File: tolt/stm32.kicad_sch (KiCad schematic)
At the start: 16 parts, among them U1 STM32F405RGTx, Y1 8m

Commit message: modified:   tolt/inter.kicad_sch 	modified:   tolt/stm32.kicad_sch
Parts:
- renumbered C12 to C10, C5 to C11, C6 to C12, C7 to C5, C8 to C6, C9 to C7, C10 to C8, C11 to C9
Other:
- moved on the sheet: C1, C10, C2, C3, C4, C5, C6, C7, C8, C9

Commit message: new file:   tolt/powerstage.kicad_sch 	modified:   tolt/stm32.kicad_sch 	modified:   tolt/tolt.kicad_pro 	modified:   tolt/tolt.kicad_sch
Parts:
- added C27, C28, C31, C32, C33, C34, C37, C38, C39: 100n, Capacitor_SMD:C_0402_1005Metric, symbol Device:C
- added C29, C36, C41: 15n, Capacitor_SMD:C_0603_1608Metric, symbol Device:C
- added C30, C35, C40: 1n, Capacitor_SMD:C_0603_1608Metric, symbol Device:C
- added R33, R34, R35: 1k, Resistor_SMD:R_0603_1608Metric, symbol Device:R
- added U10, U6, U8: MC74VHC1GT66, Package_TO_SOT_SMD:SOT-353_SC-70-5, symbol Analog_Switch:TS5A3166DCKR
- added U5, U7, U9: ~, Package_TO_SOT_SMD:SOT-23-8, symbol Amplifier_Current:INA241
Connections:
- net CURRENT_1: now also C30.1, R33.2, U10.1
- net CURRENT_2: now also C35.1, R34.2, U6.1
- net CURRENT_3: now also C40.1, R35.2, U8.1
- net GND: now also C27.1, C28.1, C29.2, C30.2, C31.1, C32.1, C33.1, C34.1, C35.2, C36.2, C37.1, C38.1, C39.1, C40.2, C41.2, U10.3 (GND), U5.2 (GND), U5.3 (REF2), U6.3 (GND), U7.2 (GND), U7.3 (REF2), U8.3 (GND), U9.2 (GND), U9.3 (REF2)
- net VCC: now also C27.2, C28.2, C31.2, C32.2, C33.2, C34.2, C37.2, C38.2, C39.2, U10.5 (V+), U5.6 (Vs), U5.7 (REF1), U6.5 (V+), U7.6 (Vs), U7.7 (REF1), U8.5 (V+), U9.6 (Vs), U9.7 (REF1)
- new net: R33.1, U5.5 (OUT)
- new net: C36.1, U6.2
- new net: R34.1, U7.5 (OUT)
- new net: C29.1, U10.2
- new net: R35.1, U9.5 (OUT)
- new net: C41.1, U8.2
- new net CURR_FILTER: U10.4, U6.4, U8.4
- new net sens_a+: U5.8 (IN+)
- new net sens_a-: U5.1 (IN-)
- new net sens_b+: U7.8 (IN+)
- new net sens_b-: U7.1 (IN-)
- new net sens_c+: U9.8 (IN+)
- new net sens_c-: U9.1 (IN-)
- no-connect marks 4 -> 7
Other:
- moved on the sheet: C1, C10, C11, C12, C13, C14, C2, C3, C4, C5, C6, C7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

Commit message: i hate RC Filters
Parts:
- added J14: BOOT0, x`, symbol Connector_Generic:Conn_01x02
- added J15: NRST, Jumper:SolderJumper-2_P1.3mm_Open_RoundedPad1.0x1.5mm, symbol Connector_Generic:Conn_01x02
- added R38, R39: 10k, Resistor_SMD:R_0603_1608Metric, symbol Device:R_Small
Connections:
- net GND: now also J15.1 (Pin_1), R38.2
- net at U1.60 (BOOT0): now also J14.2 (Pin_2), R38.1
- net at U1.7 (NRST): now also J15.2 (Pin_2), R39.2
- net sens_a+ renamed SENS_A+
- net sens_a- renamed SENS_A-
- net sens_b+ renamed SENS_B+
- net sens_b- renamed SENS_B-
- net sens_c+ renamed SENS_C+
- net sens_c- renamed SENS_C-
- new net +3V3: J14.1 (Pin_1), R39.1

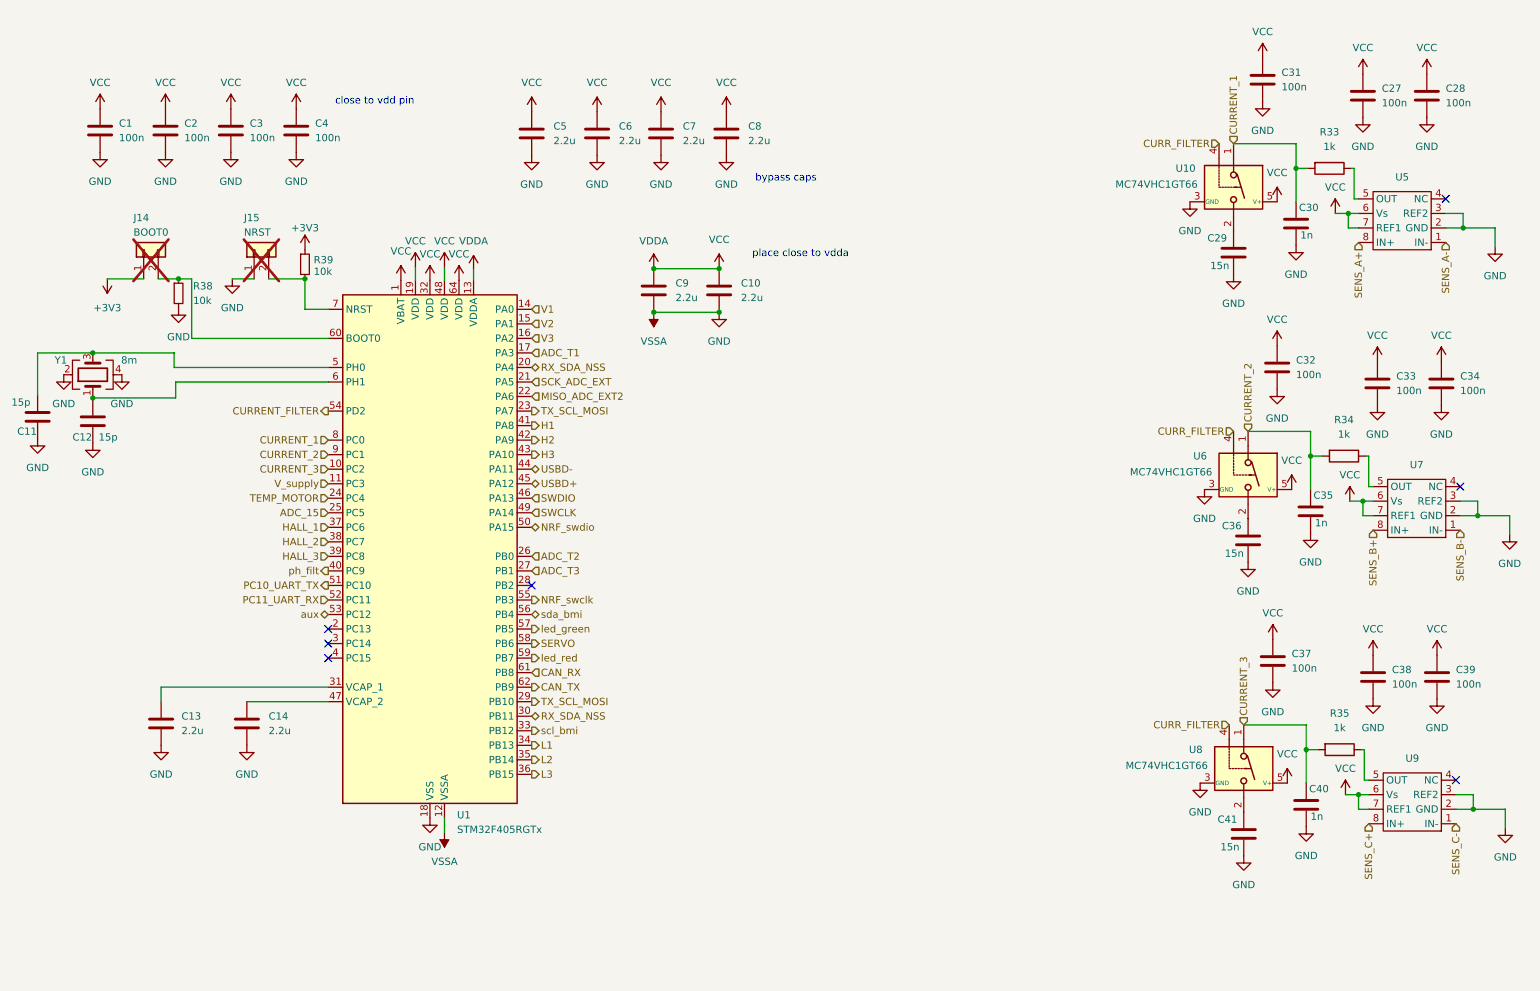
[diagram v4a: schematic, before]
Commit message: modified:   tolt/inter.kicad_sch 	modified:   tolt/stm32.kicad_sch 	modified:   tolt/tolt.kicad_sch
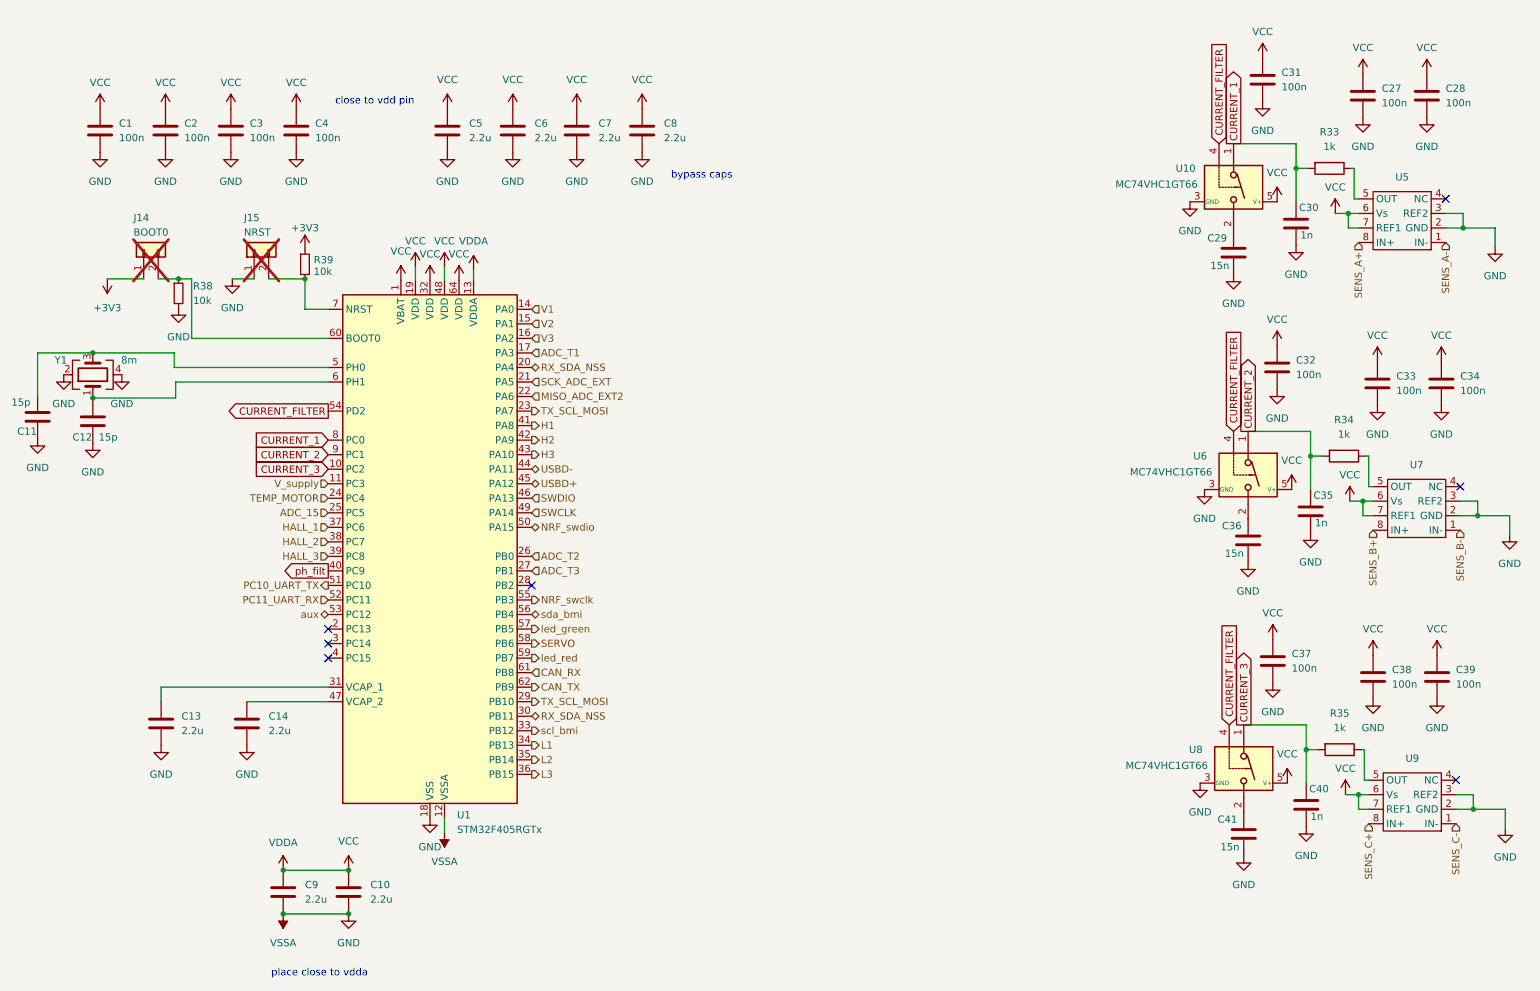
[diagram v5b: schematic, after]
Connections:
- net CURR_FILTER is gone; now on net CURRENT_FILTER: U10.4, U6.4, U8.4
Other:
- moved on the sheet: C10, C5, C6, C7, C8, C9

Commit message: modified:   tolt/inter.kicad_sch 	modified:   tolt/powerstage.kicad_sch 	modified:   tolt/stm32.kicad_sch 	modified:   tolt/tolt.kicad_sch
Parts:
- added C45, C46, C47, C48, C49, C50: 100n, Capacitor_SMD:C_0402_1005Metric, symbol Device:C
- added U11, U12, U13: MC74VHC1GT66, Package_TO_SOT_SMD:SOT-353_SC-70-5, symbol Analog_Switch:TS5A3166DCKR
- U5: value ~ -> INA240/241
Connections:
- net GND: now also C48.1, C49.1, C50.1, U11.2, U11.3 (GND), U12.2, U12.3 (GND), U13.2, U13.3 (GND)
- net V1: now also C45.2
- net V2: now also C46.2
- net V3: now also C47.2
- net VCC: now also C48.2, C49.2, C50.2, U11.5 (V+), U12.5 (V+), U13.5 (V+)
- net ph_filt: now also U11.4, U12.4, U13.4
- new net: C46.1, U12.1
- new net: C45.1, U11.1
- new net: C47.1, U13.1
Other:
- note added: "0.3mr with 20gain 0.1mr with 50gain"
- note added: "Gain 20V/V"
- moved on the sheet: C10, C9

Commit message: Converters
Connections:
- net +3V3: no longer R39.1
- net VCC: now also R39.1; no longer C9.2, U1.13 (VDDA), U5.6 (Vs), U5.7 (REF1), U7.6 (Vs), U7.7 (REF1), U9.6 (Vs), U9.7 (REF1)
- new net VDDA: C9.2, U1.13 (VDDA), U5.6 (Vs), U5.7 (REF1), U7.6 (Vs), U7.7 (REF1), U9.6 (Vs), U9.7 (REF1)

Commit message: .
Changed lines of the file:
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@@
 	)
 	(hierarchical_label "SWDIO"
-		(shape input)
+		(shape bidirectional)
 		(at 109.474 98.044 0)
 		(effects
